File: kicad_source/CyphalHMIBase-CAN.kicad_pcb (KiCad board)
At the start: 2 copper layers, 52 x 36 mm, 42 parts, among them CN1 RASPBERRYPI_PICO, CN2 SM04B-SRSS-TB, CN3 SM04B-SRSS-TB, CN4 SM04B-GHS-TB, CN5 SM04B-GHS-TB, CN7 DNI, SW1 PTS636 SM43 SMTR LFS, U3 M24C64-RMN6TP, U8 MCP2515T-I/SO, U9 SN65HVD230, Y1 X322516MLB4SI

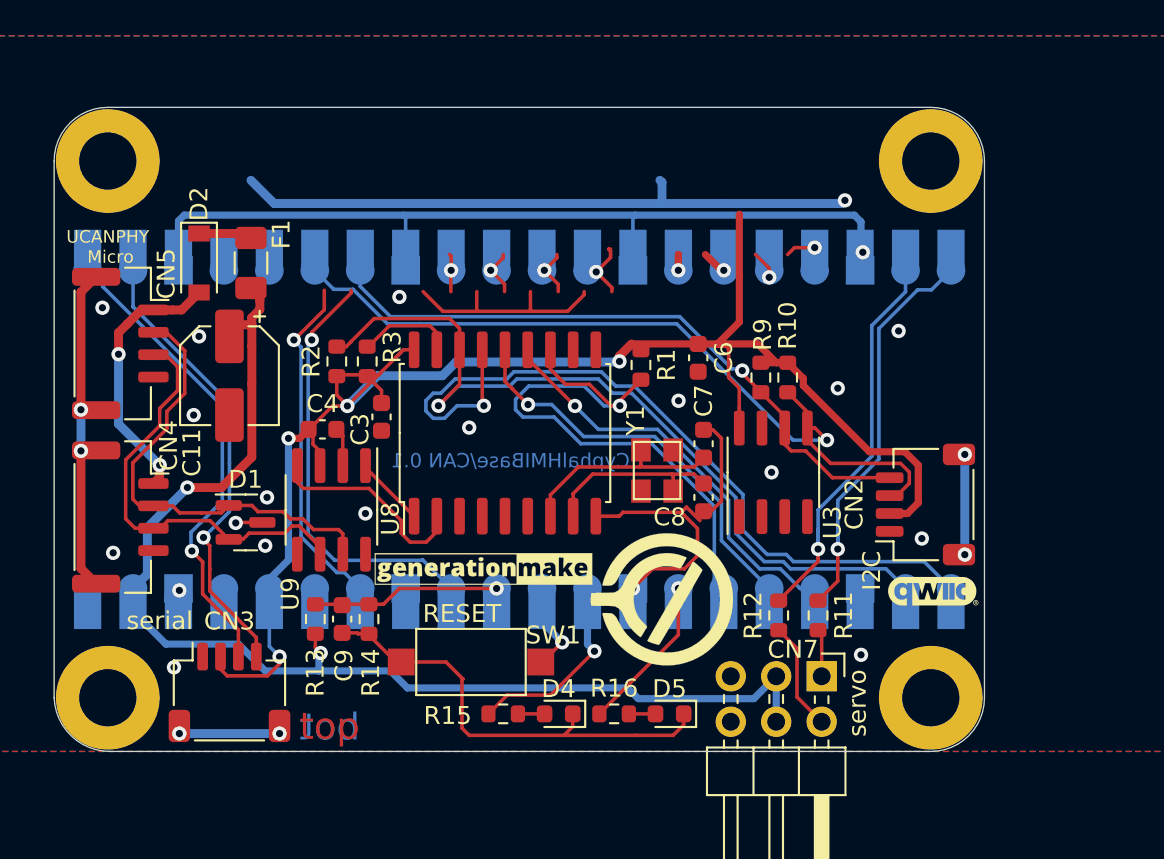
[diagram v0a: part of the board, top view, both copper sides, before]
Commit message: added display
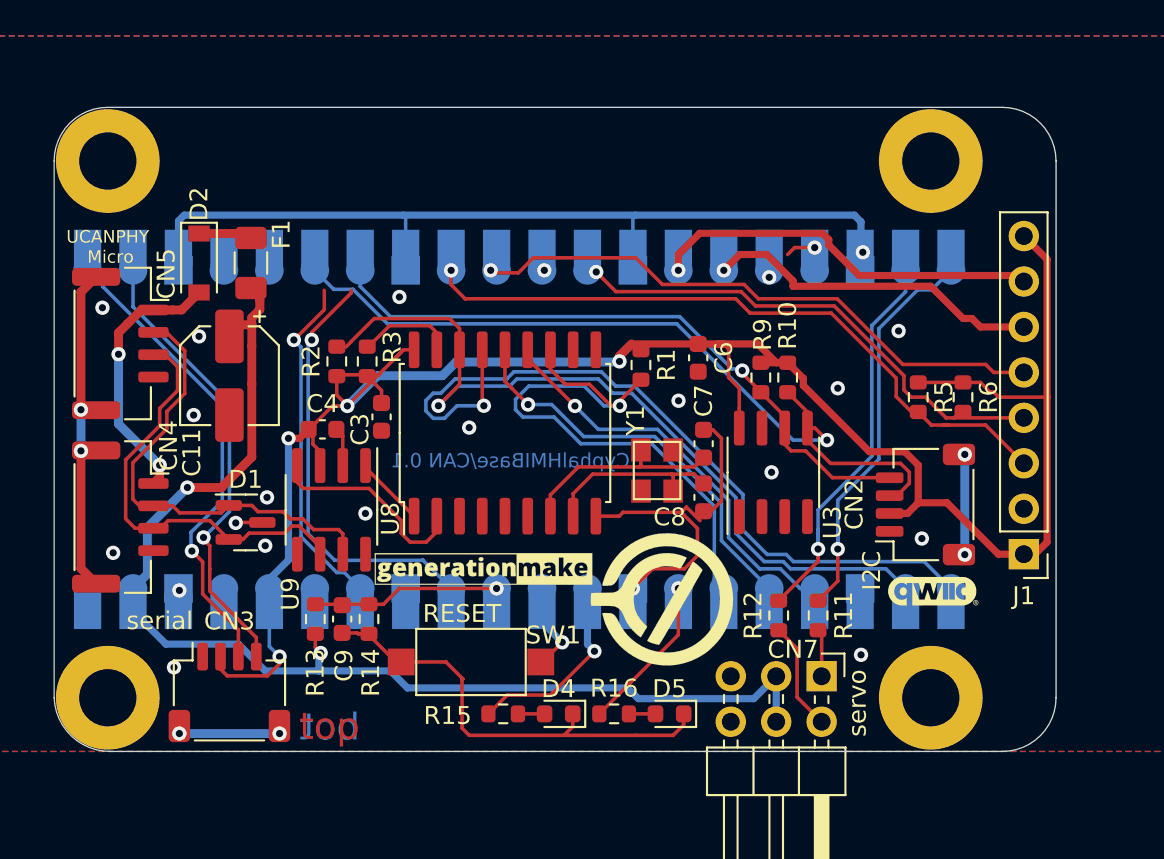
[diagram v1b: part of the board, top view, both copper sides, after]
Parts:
- added J1: Conn_01x08, Connector_PinHeader_2.54mm:PinHeader_1x08_P2.54mm_Vertical, F.Cu at (118.2, 99.0)
- added R5: 10k, Resistor_SMD:R_0603_1608Metric, F.Cu at (112.3, 90.2)
- added R6: 10k, Resistor_SMD:R_0603_1608Metric, F.Cu at (114.8, 90.2)
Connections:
- CN1 pad 10: /TFT_DC -> TFT_DC
- CN1 pad 12: /TFT_RST -> TFT_RST
- CN1 pad 14: /SPI1_CLK -> SPI1_SCK
- CN1 pad 15: /SPI1_MOSI -> SPI1_MOSI
- CN1 pad 9: /TFT_CS -> TFT_CS
- D2 pad 1: Net-(D2-K) -> (no net)
- F1 pad 2: Net-(D2-K) -> (no net)
- U9 pad 5: unconnected-(U9-NC2-Pad5) -> (no net)
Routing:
- net TFT_CS: track 0.00 -> 39.1 mm, vias 0 -> 1
- net +BATT: track 102.3 -> 67.1 mm, vias 3 -> 2
- net TFT_DC: track 0.00 -> 34.1 mm, vias 0 -> 1
- net TFT_RST: track 0.00 -> 29.7 mm, vias 0 -> 1
- net +3V3: track 90.8 -> 116.9 mm
- net SPI1_SCK: track 0.00 -> 23.2 mm, vias 0 -> 1
- net SPI1_MOSI: track 0.00 -> 20.3 mm, vias 0 -> 1
- net GND: track 106.9 -> 94.6 mm
- net /TFT_RST: track 4.49 -> 0.00 mm, vias 1 -> 0
- net Net-(D2-K): track 4.26 -> 0.00 mm
- net /TFT_DC: track 3.96 -> 0.00 mm, vias 1 -> 0
- net /TFT_CS: track 3.39 -> 0.00 mm, vias 1 -> 0
- net /SPI1_MOSI: track 2.67 -> 0.00 mm, vias 1 -> 0
- net /SPI1_CLK: track 2.16 -> 0.00 mm, vias 1 -> 0
- net /SPI1_MISO: track 2.86 -> 1.27 mm
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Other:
- board size 52 x 36 mm -> 56 x 36 mm

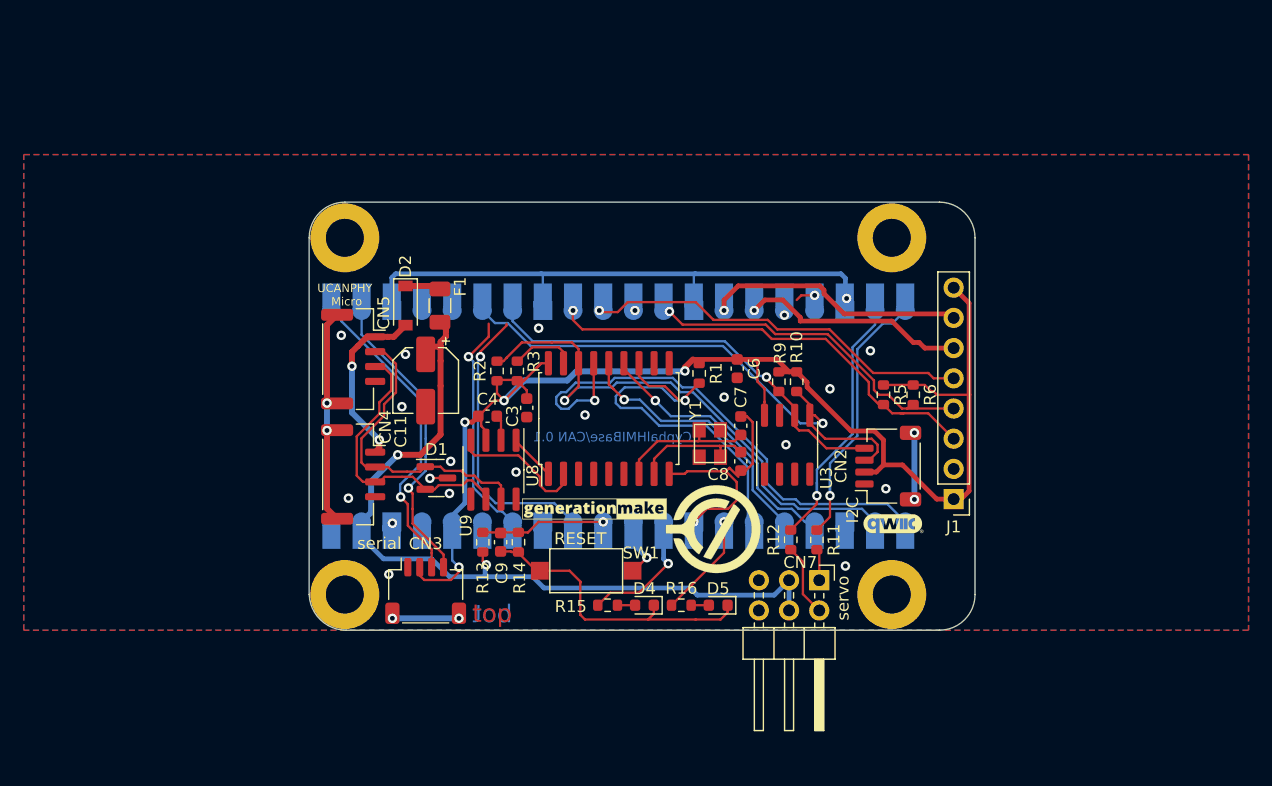
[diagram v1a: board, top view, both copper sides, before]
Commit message: added encoder, mounting holes for display at correct position
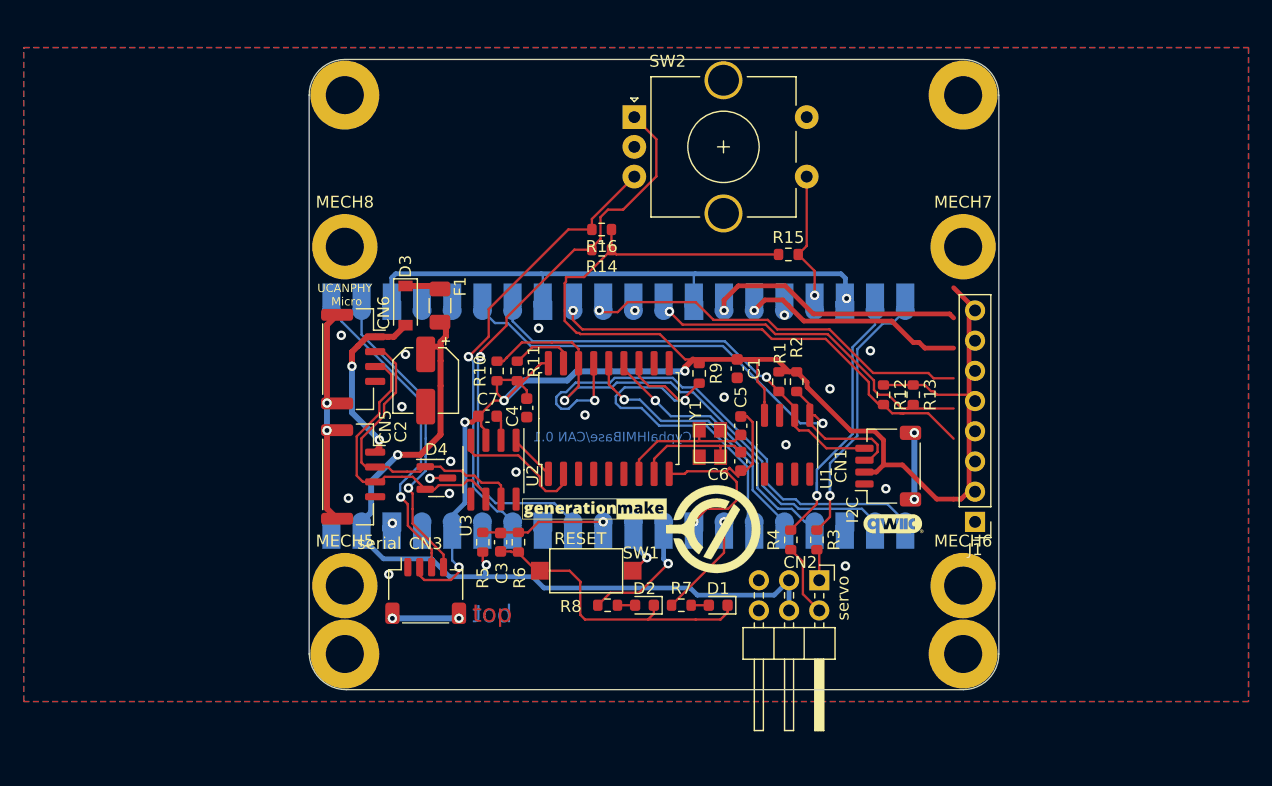
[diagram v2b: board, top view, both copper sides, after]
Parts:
- removed the R5 at (112.3, 90.2)
- removed the R6 at (114.8, 90.2)
- added MECH5: MHP_3.2_5.8, MountingHole:MountingHole_3.2mm_M3_ISO14580_Pad, F.Cu at (67.0, 106.2)
- added MECH6: MHP_3.2_5.8, MountingHole:MountingHole_3.2mm_M3_ISO14580_Pad, F.Cu at (119.0, 106.2)
- added MECH7: MHP_3.2_5.8, MountingHole:MountingHole_3.2mm_M3_ISO14580_Pad, F.Cu at (119.0, 77.8)
- added MECH8: MHP_3.2_5.8, MountingHole:MountingHole_3.2mm_M3_ISO14580_Pad, F.Cu at (67.0, 77.8)
- added R12: 10k, Resistor_SMD:R_0603_1608Metric, F.Cu at (112.3, 90.2)
- added R13: 10k, Resistor_SMD:R_0603_1608Metric, F.Cu at (114.8, 90.2)
- added R14: 10k, Resistor_SMD:R_0603_1608Metric, F.Cu at (88.6, 78.0)
- added R15: 10k, Resistor_SMD:R_0603_1608Metric, F.Cu at (104.3, 78.4)
- added R16: 10k, Resistor_SMD:R_0603_1608Metric, F.Cu at (88.6, 76.3)
- added SW2: RotaryEncoder_Switch_MP, Rotary_Encoder:RotaryEncoder_Alps_EC11E-Switch_Vertical_H20mm_CircularMountingHoles, F.Cu at (91.3, 66.8)
- moved MECH2 13.4 mm to (119.0, 65.0)
- moved MECH1 12.0 mm to (67.0, 65.0)
- moved MECH4 7.81 mm to (119.0, 112.0)
- moved MECH3 5.00 mm to (67.0, 112.0)
- moved J1 2.63 mm to (120.0, 100.9)
- renumbered C6 to C1, C11 to C2, C9 to C3, C3 to C4, C7 to C5, C8 to C6, C4 to C7, CN2 to CN1, CN7 to CN2, CN1 to CN4, CN4 to CN5, CN5 to CN6, D5 to D1, D4 to D2, D2 to D3, D1 to D4, R9 to R1, R2 to R10, R3 to R11, R10 to R2, R11 to R3, R12 to R4, R13 to R5, R14 to R6, R16 to R7, R15 to R8, R1 to R9, U3 to U1, U8 to U2, U9 to U3
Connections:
- CN4 pad 17: /ROT_SW -> ROT_SW
- CN4 pad 32: /ROT_A -> ROT_A
- CN4 pad 34: /ROT_B -> ROT_B
- D3 pad 1: (no net) -> Net-(D3-K)
- F1 pad 2: (no net) -> Net-(D3-K)
- U3 pad 5: (no net) -> unconnected-(U3-NC2-Pad5)
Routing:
- net ROT_A: track 0.00 -> 50.1 mm, vias 0 -> 1
- net ROT_B: track 0.00 -> 39.0 mm, vias 0 -> 1
- net +3V3: track 116.9 -> 153.5 mm
- net /ROT_A: track 25.1 -> 0.00 mm, vias 1 -> 0
- net /ROT_B: track 20.4 -> 0.00 mm, vias 1 -> 0
- net ROT_SW: track 0.00 -> 10.9 mm, vias 0 -> 1
- net Net-(D3-K): track 0.00 -> 4.26 mm
- net (no net): track 10.6 -> 6.35 mm
- net /ROT_SW: track 1.67 -> 0.00 mm, vias 1 -> 0
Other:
- board size 56 x 36 mm -> 58 x 53 mm

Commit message: added sd card, updated layout
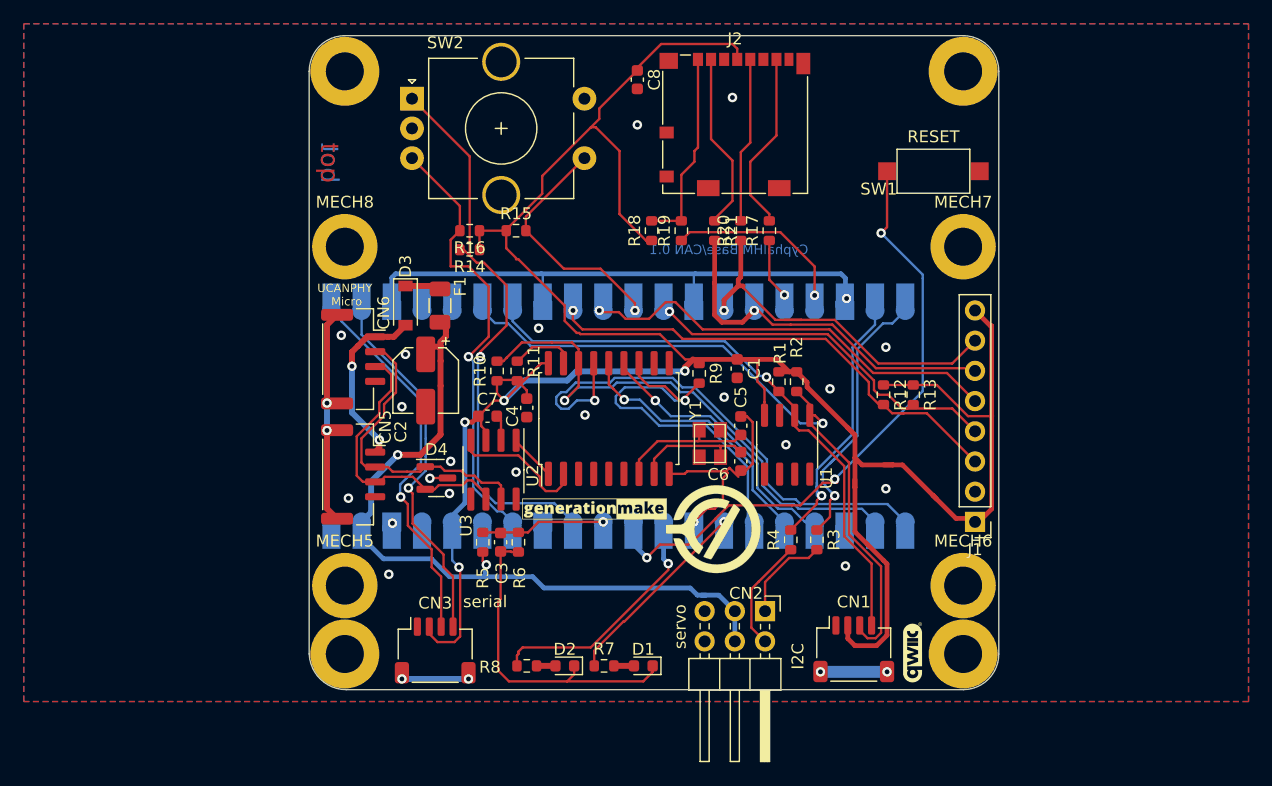
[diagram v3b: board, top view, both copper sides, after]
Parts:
- added C8: 100nF, Capacitor_SMD:C_0603_1608Metric, F.Cu at (91.6, 63.7)
- added J2: SD_Card_Device, Connector_Card:microSD_HC_Molex_104031-0811, F.Cu at (99.8, 67.4)
- added R17: 0R, Resistor_SMD:R_0603_1608Metric, F.Cu at (102.7, 76.4)
- added R18: 10k, Resistor_SMD:R_0603_1608Metric, F.Cu at (92.8, 76.4)
- added R19: 0R, Resistor_SMD:R_0603_1608Metric, F.Cu at (95.3, 76.4)
- added R20: 0R, Resistor_SMD:R_0603_1608Metric, F.Cu at (100.3, 76.4)
- added R21: 0R, Resistor_SMD:R_0603_1608Metric, F.Cu at (98.1, 76.4)
- moved SW1 44.5 mm to (116.5, 71.4), turned to 0 degrees
- moved R15 23.0 mm to (81.4, 76.4)
- moved SW2 18.8 mm to (72.7, 65.3)
- moved CN1 15.7 mm to (109.8, 111.6), turned to 0 degrees
- moved R16 11.1 mm to (77.5, 76.4)
- moved R14 11.1 mm to (77.5, 78.0)
- moved L4 11.0 mm to (114.7, 111.9), turned to 90 degrees
- moved R8 8.50 mm to (82.3, 113.0)
- moved D2 8.42 mm to (85.5, 113.0)
- moved R7 8.26 mm to (88.8, 113.0)
- moved D1 8.11 mm to (92.1, 113.0)
- moved CN2 5.25 mm to (102.3, 108.4)
- moved CN3 5.06 mm to (74.6, 111.7)
- moved MECH1 2.00 mm to (67.0, 63.0)
- moved MECH2 2.00 mm to (119.0, 63.0)
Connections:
- CN4 pad 11: unconnected-(CN4-GP8/SPI1_RX/I2C0_SDA/UART1_TX-Pad11) -> ROT_SW
- CN4 pad 16: /SPI1_MISO -> SPI1_MISO
- CN4 pad 17: ROT_SW -> SD_CS
- SW2 pad MP: unconnected-(SW2-PadMP) -> (no net)
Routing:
- net +3V3: track 153.5 -> 214.7 mm
- net /RESET: track 5.13 -> 53.2 mm, vias 1 -> 3
- net /SD Card/SD_CS_R: track 0.00 -> 16.7 mm
- net /SD Card/SPI1_MISO_R: track 0.00 -> 15.2 mm
- net SD_CS: track 0.00 -> 15.1 mm, vias 0 -> 1
- net /SD Card/SPI1_MOSI_R: track 0.00 -> 14.9 mm
- net /I2C_SDA: track 46.8 -> 61.1 mm
- net /SD Card/SPI1_SCK_R: track 0.00 -> 13.9 mm
- net /I2C_SCL: track 37.2 -> 50.5 mm
- net SPI1_MOSI: track 20.1 -> 32.2 mm
- net ROT_SW: track 10.9 -> 21.7 mm
- net /LED3: track 11.0 -> 20.9 mm
- net SPI1_SCK: track 23.1 -> 32.6 mm
- net /LED2: track 10.1 -> 17.9 mm
- net SPI1_MISO: track 0.00 -> 6.37 mm, vias 0 -> 1
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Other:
- board size 58 x 53 mm -> 58 x 55 mm

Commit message: added push button
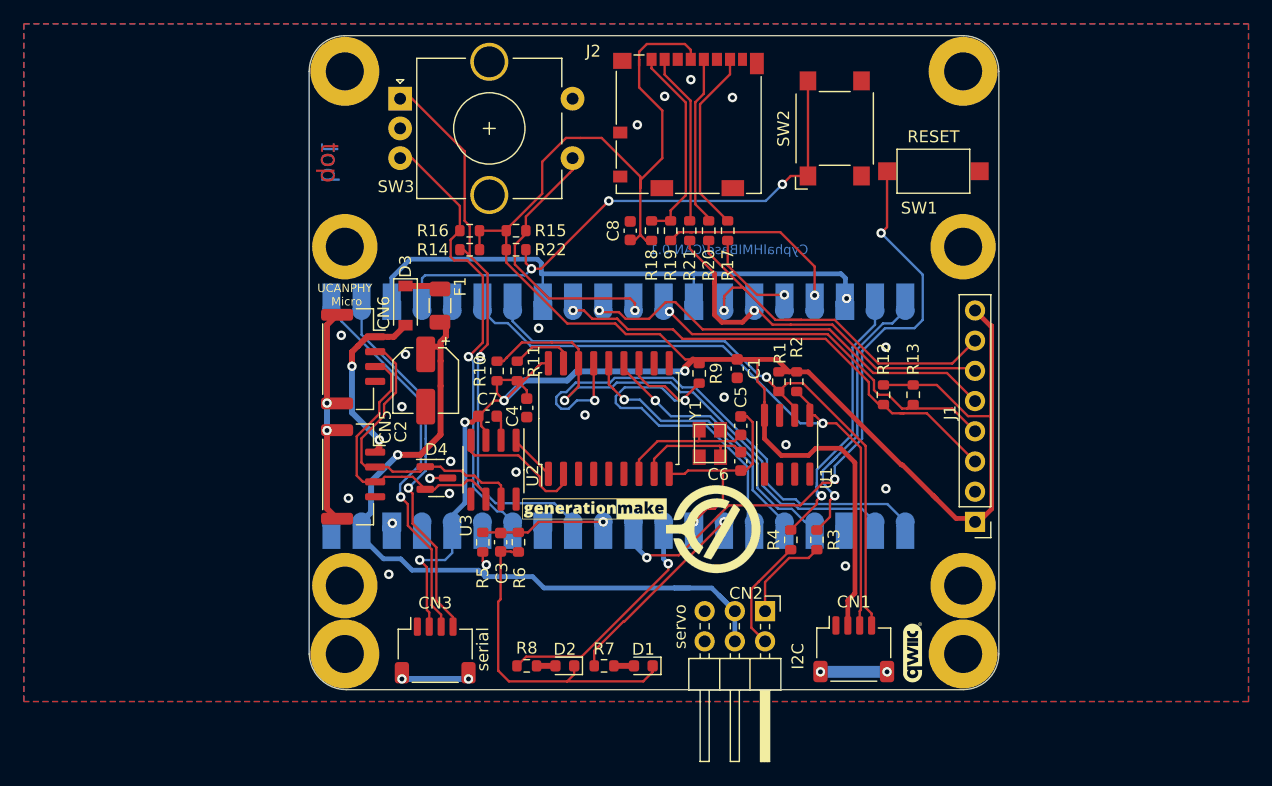
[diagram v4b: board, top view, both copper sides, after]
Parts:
- added R22: 10k, Resistor_SMD:R_0603_1608Metric, F.Cu at (81.4, 78.0)
- added SW2: SW_Push, Button_Switch_SMD:SW_SPST_Omron_B3FS-100xP, F.Cu at (108.2, 67.8)
- moved C8 12.7 mm to (91.0, 76.4), turned to 90 degrees
- moved J2 3.91 mm to (95.9, 67.4)
- moved R17 3.50 mm to (99.2, 76.4)
- moved R20 2.70 mm to (97.6, 76.4)
- moved R21 2.10 mm to (96.0, 76.4)
- moved SW3 1.00 mm to (71.7, 65.3)
- moved R19 0.90 mm to (94.4, 76.4)
- renumbered SW2 to SW3
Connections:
- CN4 pad 4: unconnected-(CN4-GP2/SPI0_SCK/I2C1_SDA-Pad4)_1 -> SWITCH1
- SW3 pad MP: (no net) -> unconnected-(SW3-PadMP)
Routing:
- net SWITCH1: track 0.00 -> 48.5 mm, vias 0 -> 3
- net /I2C_SCL: track 50.5 -> 54.7 mm
- net /I2C_SDA: track 61.1 -> 57.8 mm
- net +BATT: track 63.0 -> 65.9 mm
- net SPI1_MISO: track 6.37 -> 9.16 mm
- net ROT_SW: track 21.7 -> 24.3 mm
- net +3V3: track 214.7 -> 216.7 mm
- net SPI1_SCK: track 32.6 -> 34.1 mm
- net /RESET: track 53.2 -> 54.5 mm
- net (no net): track 5.08 -> 3.81 mm
- net GND: track 95.5 -> 96.7 mm, vias 22 -> 23
- net SD_CS: track 15.1 -> 16.2 mm
- net SPI1_MOSI: track 32.2 -> 33.1 mm
- net ROT_A: track 48.7 -> 48.1 mm
- net /LED3: track 20.9 -> 20.3 mm
